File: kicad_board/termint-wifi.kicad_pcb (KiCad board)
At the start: 2 copper layers, 118.9 x 33.9 mm, 20 parts, among them J1 Conn_01x04_Male, J2 Conn_01x08, J3 Conn_01x08

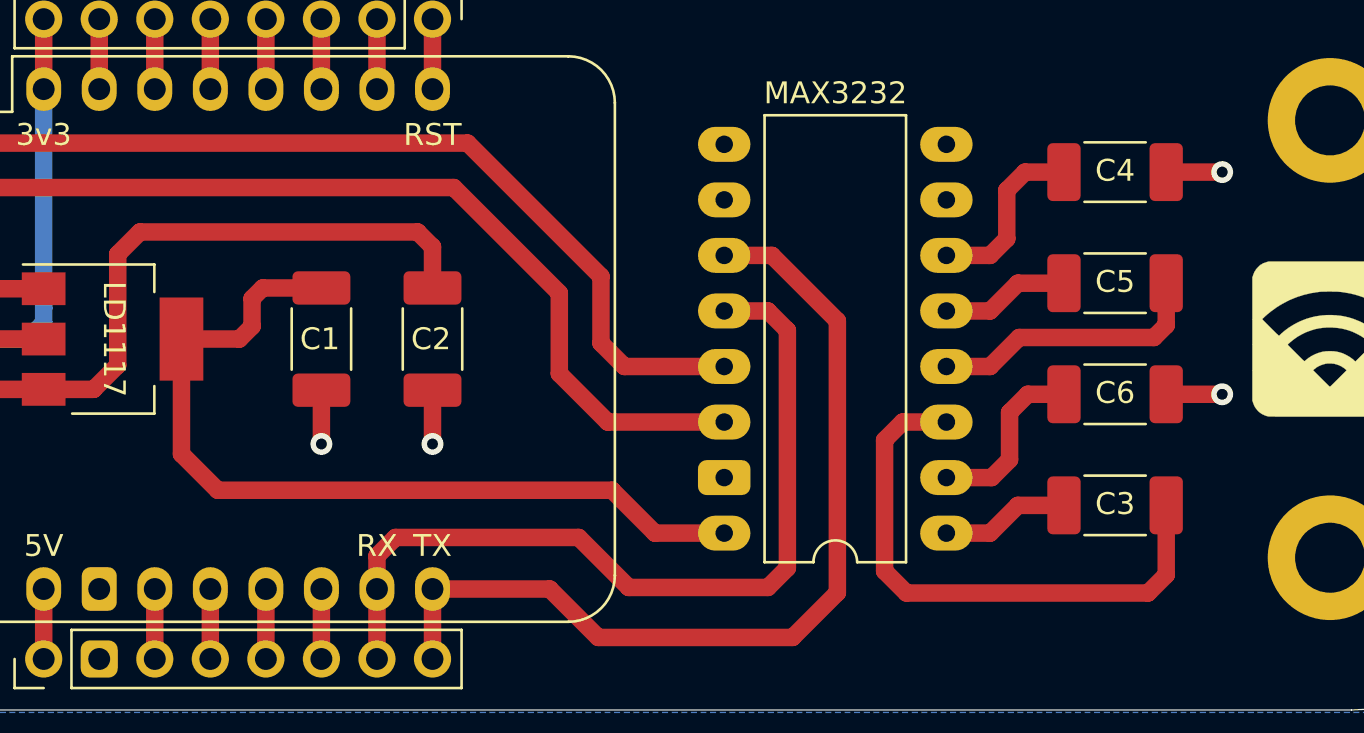
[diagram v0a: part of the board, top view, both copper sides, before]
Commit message: Changed capacitor package sizes
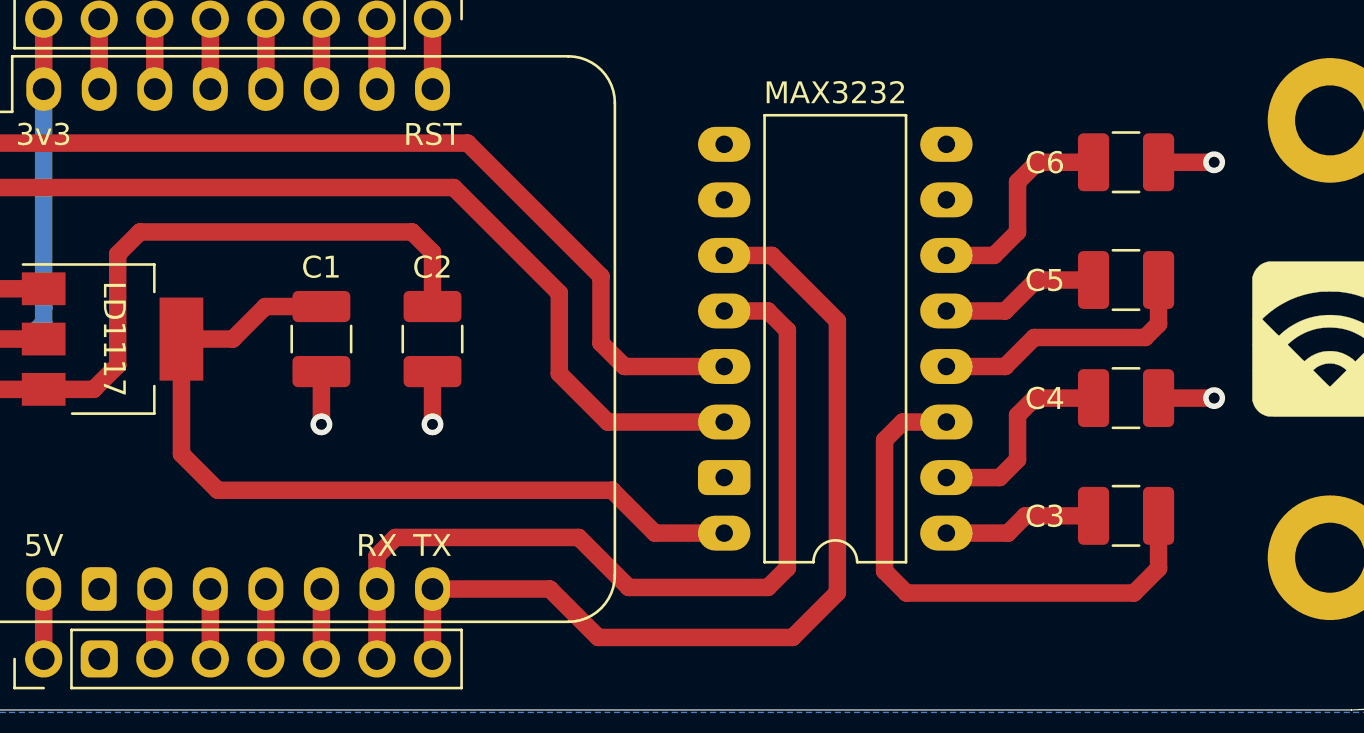
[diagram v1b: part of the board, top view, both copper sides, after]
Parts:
- C1, C2, C3, C5: footprint Capacitor_SMD:C_2010_5025Metric_Pad1.52x2.65mm_HandSolder -> Capacitor_SMD:C_1210_3225Metric_Pad1.42x2.65mm_HandSolder
- C4: renamed from C6; footprint Capacitor_SMD:C_2010_5025Metric_Pad1.52x2.65mm_HandSolder -> Capacitor_SMD:C_1210_3225Metric_Pad1.42x2.65mm_HandSolder
- C6: renamed from C4; footprint Capacitor_SMD:C_2010_5025Metric_Pad1.52x2.65mm_HandSolder -> Capacitor_SMD:C_1210_3225Metric_Pad1.42x2.65mm_HandSolder
- moved C3 0.69 mm to (153.2, 75.1)
- moved C6 0.67 mm to (153.2, 58.9)
- moved C4 0.53 mm to (153.2, 69.7)
- moved C5 0.52 mm to (153.2, 64.3)
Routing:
- net Net-(C6-Pad1): track 8.25 -> 9.83 mm
- net Net-(C5-Pad2): track 5.90 -> 7.31 mm
- net Net-(C4-Pad1): track 8.22 -> 9.42 mm
- net Net-(C3-Pad1): track 5.90 -> 7.05 mm
- net Net-(C1-Pad1): track 59.3 -> 58.3 mm
- net Net-(C3-Pad2): track 26.0 -> 25.0 mm
- net Net-(C2-Pad1): track 57.4 -> 58.1 mm

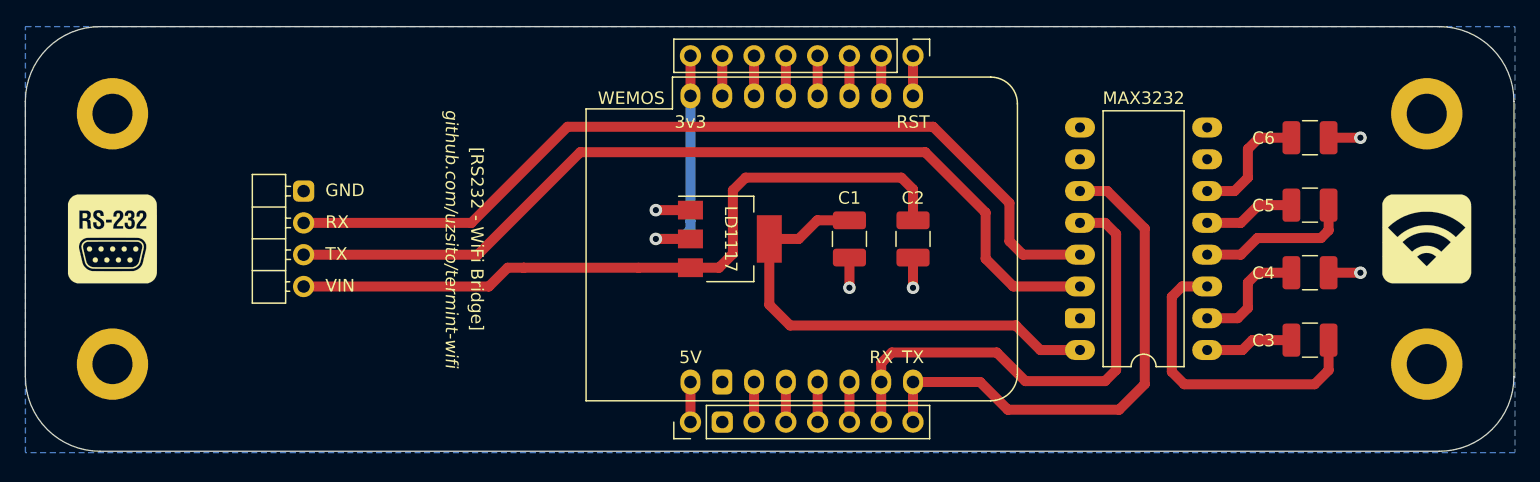
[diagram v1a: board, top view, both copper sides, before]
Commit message: Major changes: -made max3232 switchable on GPIO5. This prevents boot problems due to Wemos TX pulling low, because you can only turn on MAX3232 from code, past boot sequence. -added max3232 power indicator LED -switched SMD sizes to 1206 package
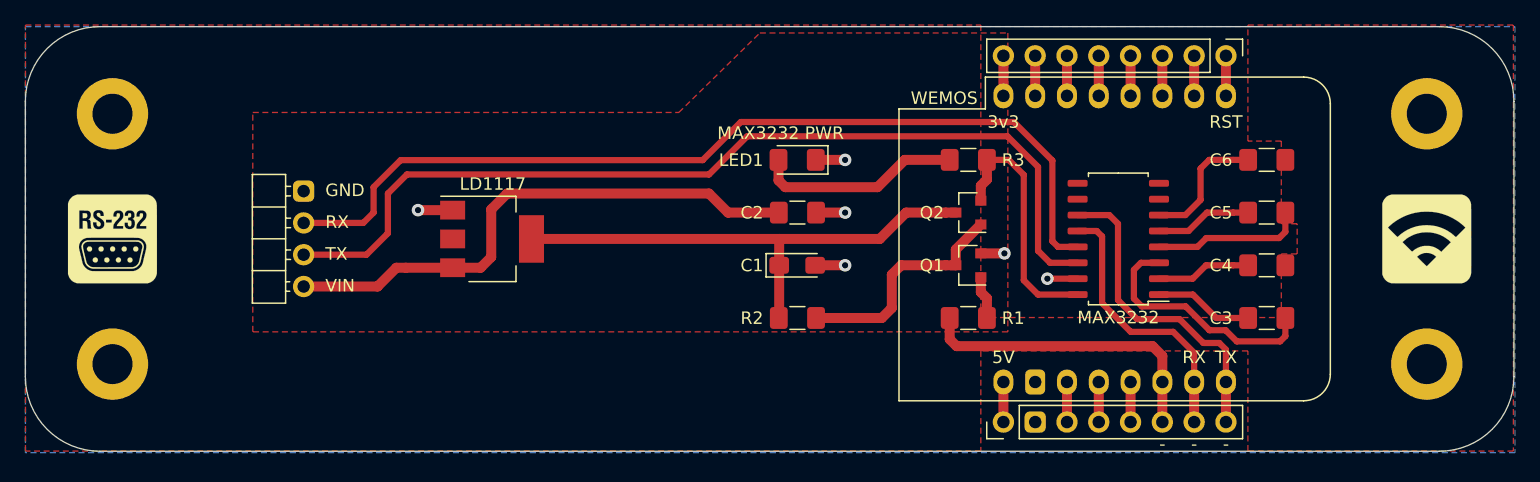
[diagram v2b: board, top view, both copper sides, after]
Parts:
- added LED1: LED, LED_SMD:LED_1206_3216Metric_Pad1.42x1.75mm_HandSolder, F.Cu at (112.2, 60.7)
- added Q1: MMBT3904, Package_TO_SOT_SMD:SOT-23, F.Cu at (125.9, 69.1)
- added Q2: AO3401A, Package_TO_SOT_SMD:SOT-23, F.Cu at (125.9, 64.9)
- added R1: 100k, Resistor_SMD:R_1206_3216Metric_Pad1.42x1.75mm_HandSolder, F.Cu at (125.9, 73.3)
- added R2: 10k, Resistor_SMD:R_1206_3216Metric_Pad1.42x1.75mm_HandSolder, F.Cu at (112.2, 73.3)
- added R3: 130R, Resistor_SMD:R_1206_3216Metric_Pad1.42x1.75mm_HandSolder, F.Cu at (125.9, 60.7)
- C1: footprint Capacitor_SMD:C_1210_3225Metric_Pad1.42x2.65mm_HandSolder -> Capacitor_Tantalum_SMD:CP_EIA-3216-12_Kemet-S_Pad1.58x1.35mm_HandSolder
- C2, C3, C4, C5, C6: footprint Capacitor_SMD:C_1210_3225Metric_Pad1.42x2.65mm_HandSolder -> Capacitor_SMD:C_1206_3216Metric_Pad1.42x1.75mm_HandSolder
- MAX3232: footprint Package_DIP:DIP-16_W10.16mm_LongPads -> Package_SO:SOIC-16_4.55x10.3mm_P1.27mm
- moved J2 25.0 mm to (146.5, 52.4)
- moved J3 25.0 mm to (128.7, 81.6)
- moved WEMOS_D1 25.0 mm to (146.5, 55.6)
- moved LD1117 19.0 mm to (87.8, 67.0)
- moved G*** 16.5 mm to (125.7, 67.5)
- moved MAX3232 11.4 mm to (137.9, 67.0)
- moved C2 9.47 mm to (112.2, 64.9), turned to 0 degrees
- moved C1 4.68 mm to (112.2, 69.1), turned to 0 degrees
- moved C6 3.88 mm to (149.7, 60.7)
- moved C3 3.88 mm to (149.7, 73.3)
- moved C4 3.51 mm to (149.7, 69.1)
- moved C5 3.51 mm to (149.7, 64.9)
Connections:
- MAX3232 pad 16: Net-(C1-Pad1) -> Net-(MAX3232-Pad16)
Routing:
- net Net-(J3-Pad6): track 3.20 -> 24.5 mm
- net Net-(MAX3232-Pad16): track 0.00 -> 20.1 mm
- net Net-(Q1-Pad3): track 0.00 -> 18.6 mm
- net Net-(J3-Pad7): track 39.3 -> 22.0 mm
- net Net-(J3-Pad8): track 42.3 -> 25.7 mm
- net Net-(LED1-Pad2): track 0.00 -> 16.4 mm
- net Net-(C2-Pad1): track 58.1 -> 43.9 mm
- net Net-(C1-Pad1): track 58.3 -> 44.3 mm, vias 1 -> 0
- net Net-(C3-Pad2): track 25.0 -> 19.7 mm
- net Net-(J1-Pad2): track 72.0 -> 75.7 mm
- net Net-(Q1-Pad1): track 0.00 -> 3.46 mm
- net Net-(J1-Pad3): track 71.2 -> 74.3 mm
- net Net-(C4-Pad1): track 9.42 -> 7.57 mm
- net GND: track 12.7 -> 14.1 mm, vias 5 -> 6
- net Net-(C3-Pad1): track 7.05 -> 7.90 mm
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- added copper zone on F.Cu, net GND
- added copper zone on F.Cu, net Net-(C1-Pad1)
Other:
- board text added: "-"
- board text added: "MAX3232 PWR"
- board text removed: "[RS232 - WiFi Bridge]"
- board text removed: "github.com/uzsito/termint-wifi"
